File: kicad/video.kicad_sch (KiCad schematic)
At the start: 15 parts, among them P10 LED_DIN, P11 5V, P12 GND, P5 CAM1_VID, P6 CAM2_VID, P7 VTX_VID, P8 5V, P9 GND, U11 TS5A3159A, U12 SN74LV1T125

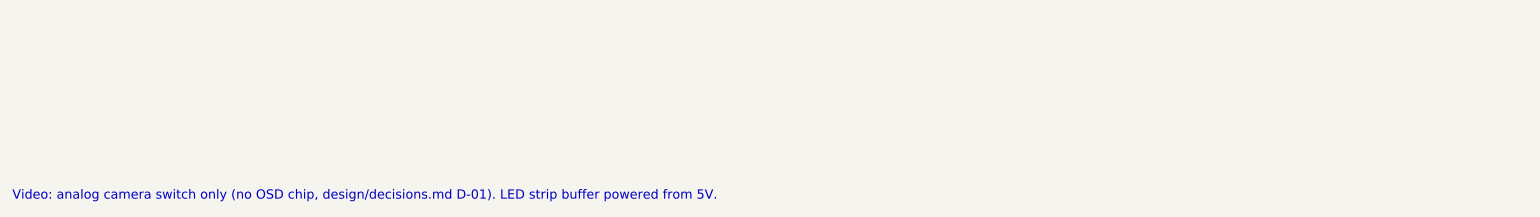
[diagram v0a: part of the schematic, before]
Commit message: Gate 1 fixes (crystal gm evidence, LDO output ESR, X7R caps, 50V HF cap, per-MPN datasheets, in_bom flags, project-file merge, parity fields), power re-audit fixes (board-level thermal envelope, USB inrush deviation, R41 VTX 0R link), PCB placement + legalizer + grommet keepouts; Gate 1 reports
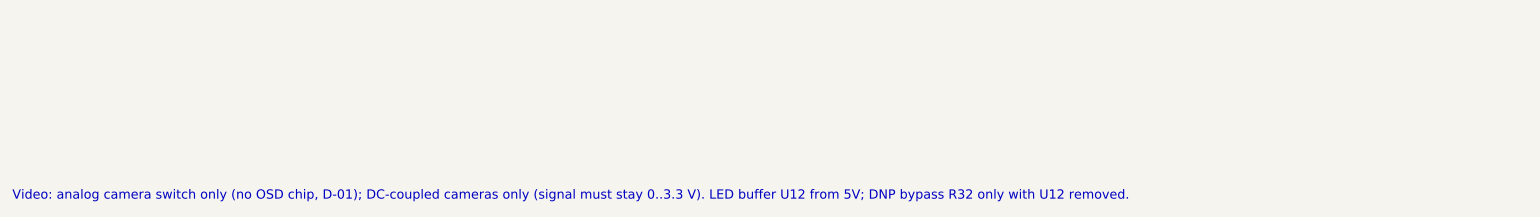
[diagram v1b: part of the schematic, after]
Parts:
- P10, P11, P12, P5, P6, P7, P8, P9: now left out of the parts list
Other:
- note added: "Video: analog camera switch only (no OSD chip, D-01); DC-coupled cameras only (signal must stay 0..3.3 V). LED buffer U12 from 5V; DNP bypass R32 only with U12 removed."
- note removed: "Video: analog camera switch only (no OSD chip, design/decisions.md D-01). LED strip buffer powered from 5V."
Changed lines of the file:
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@@
 			)
 		)
-		(property "Datasheet" "https://product.samsungsem.com/mlcc/"
+		(property "Datasheet" "https://product.samsungsem.com/mlcc/CL05B104KO5NNNC.do"
 			(at 71.12 35.56 0)
 			(effects
@@
 		(unit 1)
 		(exclude_from_sim no)
-		(in_bom yes)
+		(in_bom no)
 		(on_board yes)
 		(dnp no)
@@
 		(unit 1)
 		(exclude_from_sim no)
-		(in_bom yes)
+		(in_bom no)
 		(on_board yes)
 		(dnp no)
@@
 		(unit 1)
 		(exclude_from_sim no)
-		(in_bom yes)
+		(in_bom no)
 		(on_board yes)
 		(dnp no)
@@
 		(unit 1)
 		(exclude_from_sim no)
-		(in_bom yes)
+		(in_bom no)
 		(on_board yes)
 		(dnp no)
@@
 		(unit 1)
 		(exclude_from_sim no)
-		(in_bom yes)
+		(in_bom no)
 		(on_board yes)
 		(dnp no)
@@
 			)
 		)
-		(property "Datasheet" "https://product.samsungsem.com/mlcc/"
+		(property "Datasheet" "https://product.samsungsem.com/mlcc/CL05B104KO5NNNC.do"
 			(at 86.36 63.5 0)
 			(effects
@@
 		(unit 1)
 		(exclude_from_sim no)
-		(in_bom yes)
+		(in_bom no)
 		(on_board yes)
 		(dnp no)
@@
 		(unit 1)
 		(exclude_from_sim no)
-		(in_bom yes)
+		(in_bom no)
 		(on_board yes)
 		(dnp no)
@@
 		(unit 1)
 		(exclude_from_sim no)
-		(in_bom yes)
+		(in_bom no)
 		(on_board yes)
 		(dnp no)
@@
 		)
 	)
-	(text "Video: analog camera switch only (no OSD chip, design/decisions.md D-01). LED strip buffer powered from 5V."
+	(text "Video: analog camera switch only (no OSD chip, D-01); DC-coupled cameras only (signal must stay 0..3.3 V). LED buffer U12 from 5V; DNP bypass R32 only with U12 removed."
 		(exclude_from_sim no)
 		(at 15.24 198 0)

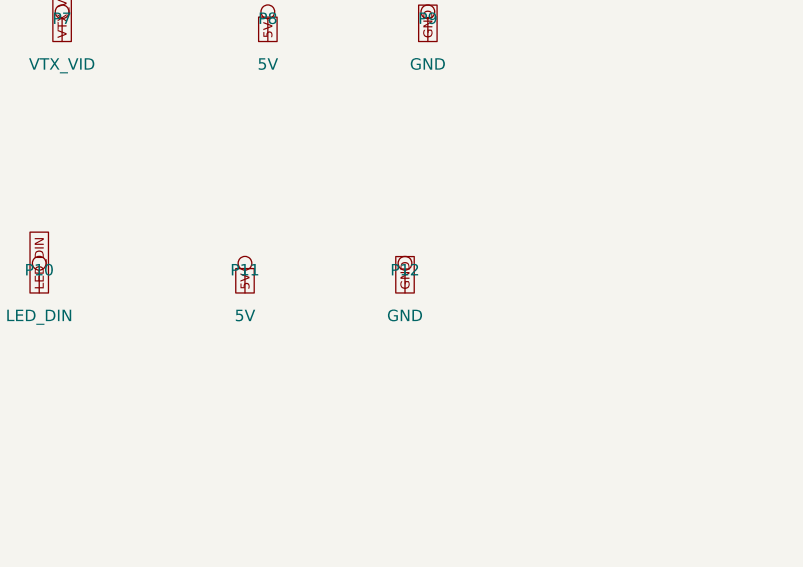
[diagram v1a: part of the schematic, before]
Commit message: Gate 3 re-review fixes: rule-based labels + regular pad grids, VBAT In2 zone, MCU routing ring/decap offsets, U13/D9 moves, P12 removed (D-21)
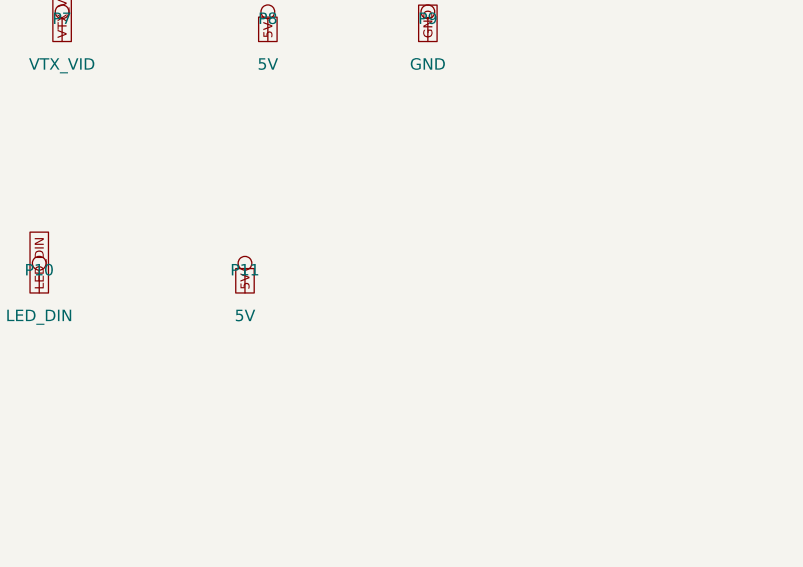
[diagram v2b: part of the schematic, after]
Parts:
- removed P12: GND, F405FC:Pad_SMD_1.5x2.0mm, symbol Connector:TestPoint
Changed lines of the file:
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@@
-		)
-	)
-	(symbol
-		(lib_id "Connector:TestPoint")
-		(at 218.44 58.42 0)
-		(unit 1)
-		(exclude_from_sim no)
-		(in_bom no)
-		(on_board yes)
-		(dnp no)
-		(property "Reference" "P12"
-			(at 218.44 55.88 0)
-			(effects
-				(font
-					(size 1.27 1.27)
-				)
-			)
-		)
-		(property "Value" "GND"
-			(at 218.44 60.96 0)
-			(effects
-				(font
-					(size 1.27 1.27)
-				)
-			)
-		)
-		(property "Footprint" "F405FC:Pad_SMD_1.5x2.0mm"
-			(at 218.44 58.42 0)
-			(effects
-				(font
-					(size 1.27 1.27)
-				)
-				(hide yes)
-			)
-		)
-		(property "Datasheet" ""
-			(at 218.44 58.42 0)
-			(effects
-				(font
-					(size 1.27 1.27)
-				)
-				(hide yes)
-			)
-		)
-		(property "Description" "LED strip pad"
-			(at 218.44 58.42 0)
-			(effects
-				(font
-					(size 1.27 1.27)
-				)
-				(hide yes)
-			)
-		)
-		(property "MPN" "n/a (PCB pad)"
-			(at 218.44 58.42 0)
-			(effects
-				(font
-					(size 1.27 1.27)
-				)
-				(hide yes)
-			)
-		)
-		(property "Manufacturer" "n/a"
-			(at 218.44 58.42 0)
-			(effects
-				(font
-					(size 1.27 1.27)
-				)
-				(hide yes)
-			)
-		)
-		(property "DigiKey" "n/a (PCB pad)"
-			(at 218.44 58.42 0)
-			(effects
-				(font
-					(size 1.27 1.27)
-				)
-				(hide yes)
-			)
-		)
-		(property "InBOM" "no"
-			(at 218.44 58.42 0)
-			(effects
-				(font
-					(size 1.27 1.27)
-				)
-				(hide yes)
-			)
-		)
-		(pin "1"
-		)
-		(instances
-			(project "F405FC"
-				(path "/85397873-de58-5f94-9eed-9a7928bbcb45/2044f6dd-e7bb-58bb-b615-40e24245c19a"
-					(reference "P12")
-					(unit 1)
-				)
-			)
-		)
-	)
-	(global_label "GND"
-		(shape passive)
-		(at 218.44 58.42 270)
-		(effects
-			(font
-				(size 1 1)
-			)
-			(justify left)
-		)
-		(property "Intersheetrefs" "${INTERSHEET_REFS}"
-			(at 218.44 58.42 0)
-			(effects
-				(font
-					(size 1.27 1.27)
-				)
-				(hide yes)
-			)
 		)
 	)

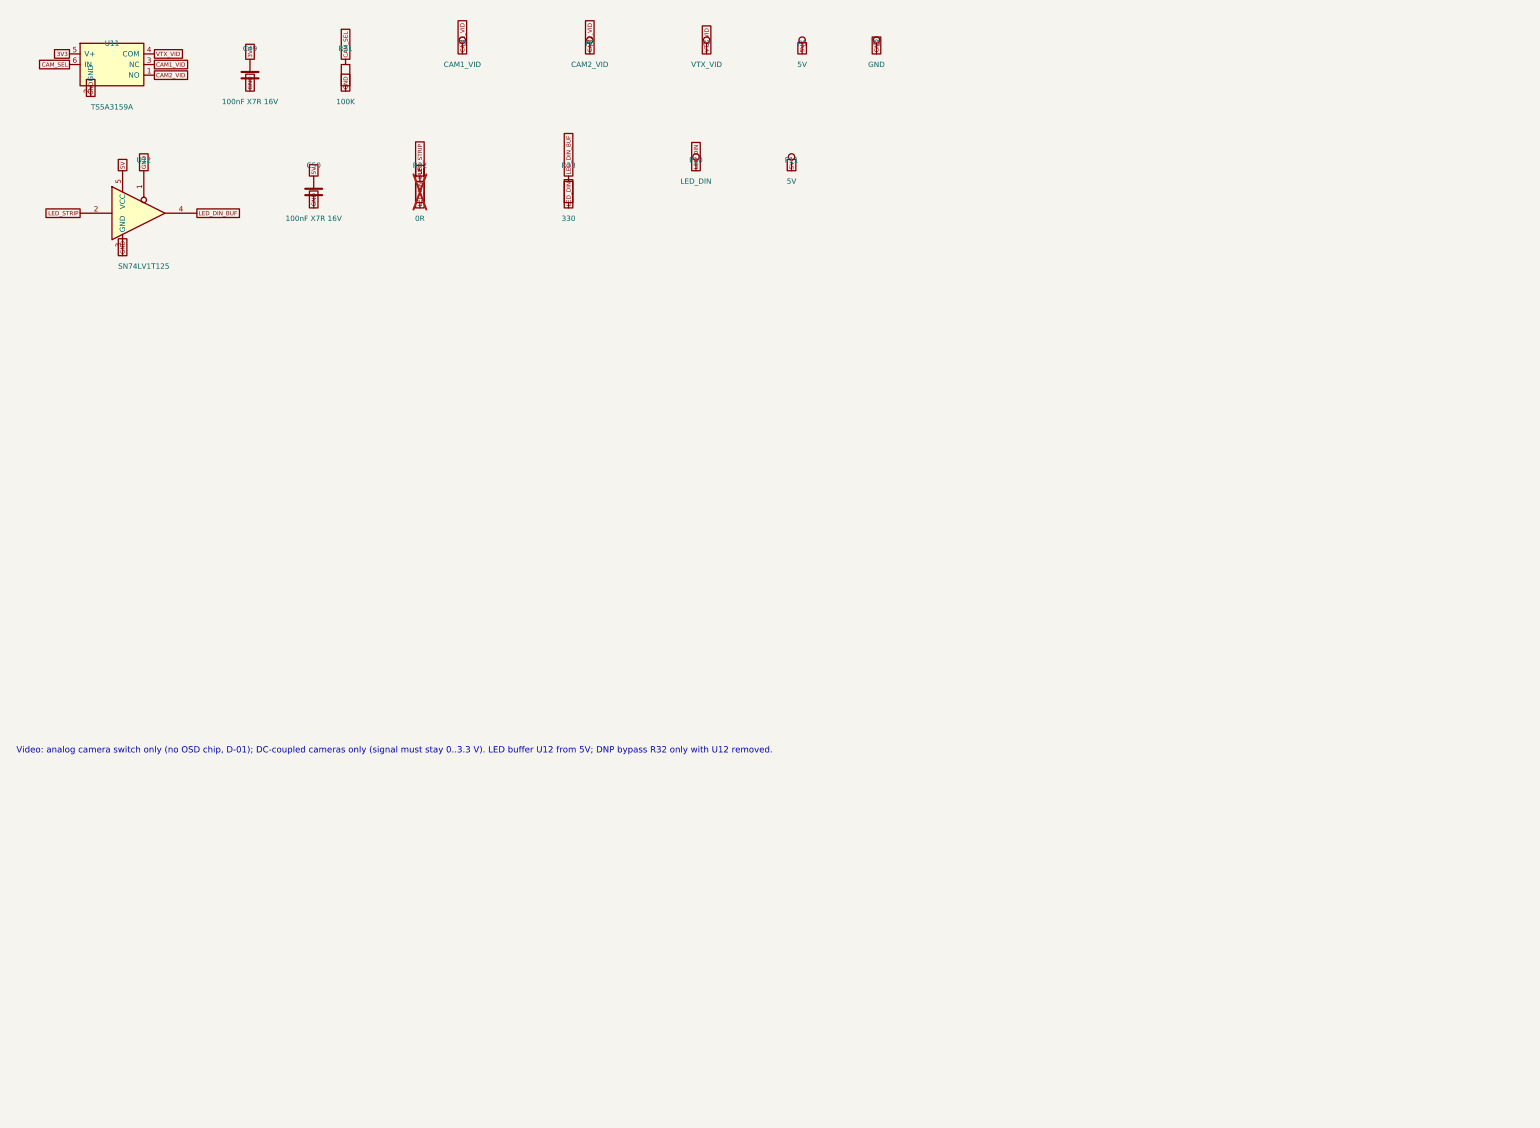
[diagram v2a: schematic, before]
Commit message: Readable schematic: functional blocks with titles, passives wired to their IC pins, GND power symbols, per-rail decoupling banks, labels only between blocks (ERC 0, netcheck OK, same nets)
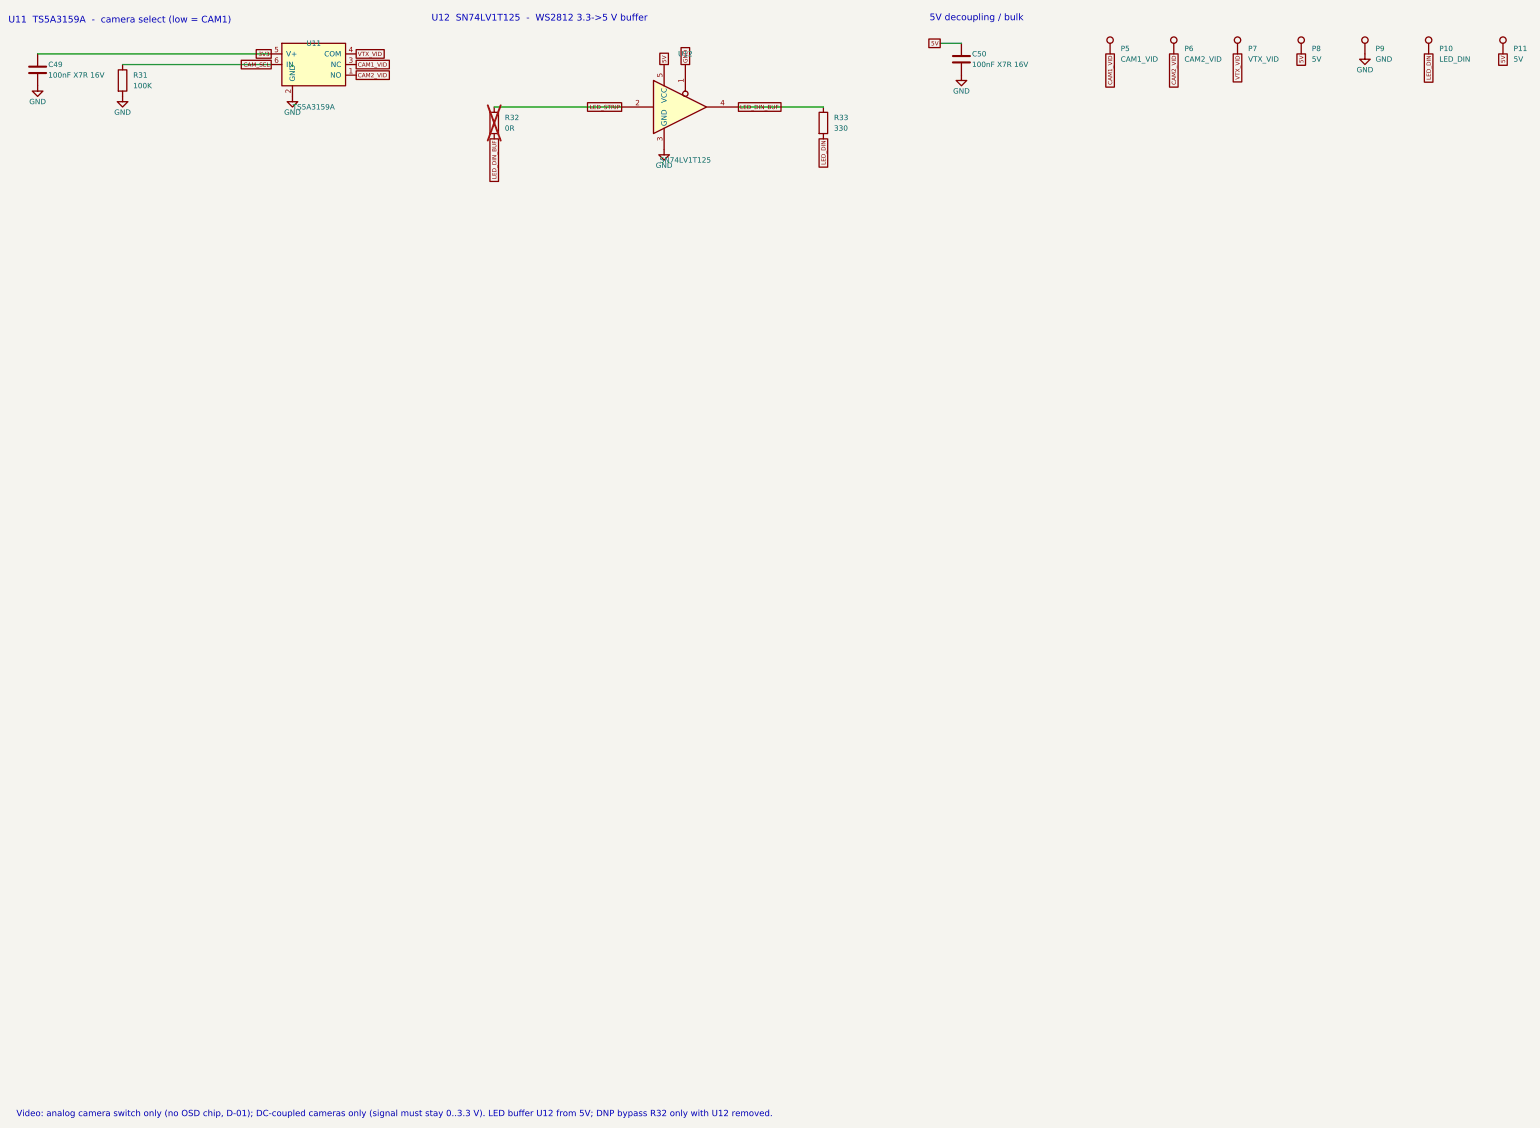
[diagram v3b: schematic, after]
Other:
- note added: "5V decoupling / bulk"
- note added: "U11 TS5A3159A - camera select (low = CAM1)"
- note added: "U12 SN74LV1T125 - WS2812 3.3->5 V buffer"
- moved on the sheet: C49, C50, P10, P11, P5, P6, P7, P8, P9, R31, R32, R33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
